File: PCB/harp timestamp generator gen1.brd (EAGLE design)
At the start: 33 x 22 mm, 11 parts, among them IC1 ATXMEGAxxxA4U-AU

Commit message: Updated R1 to 910 ohms.
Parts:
- R1: value 330 -> 910
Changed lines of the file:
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@@
 <attribute name="VALUE" x="32.2834" y="44.831" size="1.27" layer="27"/>
 </element>
-<element name="R1" library="rcl" library_urn="urn:adsk.eagle:library:334" package="R0402" package3d_urn="urn:adsk.eagle:package:23547/3" value="330" x="36.1696" y="46.736" smashed="yes" rot="R180">
+<element name="R1" library="rcl" library_urn="urn:adsk.eagle:library:334" package="R0402" package3d_urn="urn:adsk.eagle:package:23547/3" value="910" x="36.1696" y="46.736" smashed="yes" rot="R180">
 <attribute name="NAME" x="37.084" y="48.1457" size="0.8128" layer="25" font="vector" ratio="12" rot="R180"/>
 <attribute name="POPULARITY" value="0" x="36.1696" y="46.736" size="1.778" layer="27" rot="R180" display="off"/>

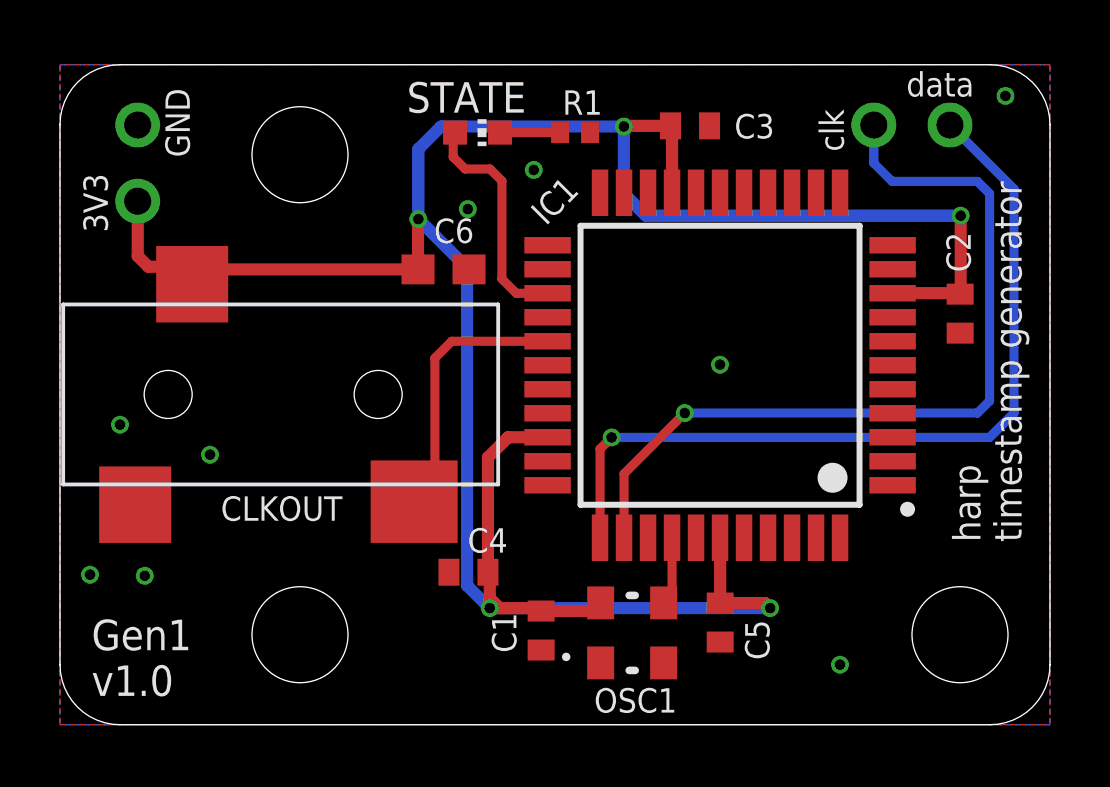
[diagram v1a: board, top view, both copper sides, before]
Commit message: Re-designed oscillator footprint for easier manual assembly
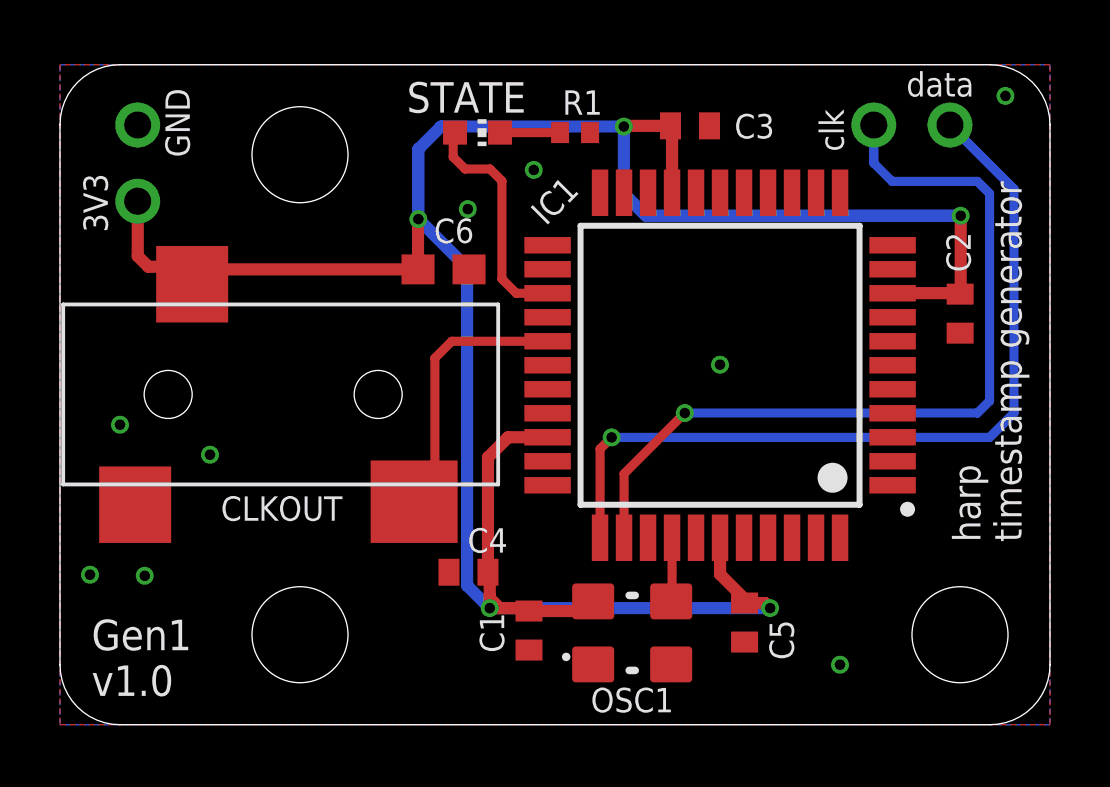
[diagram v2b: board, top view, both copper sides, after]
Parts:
- OSC1: value (none) -> CNP-MISCELLANEOUS_OSCILLATOR; device CNP-miscellaneous:OSCILLATOR_3.2X2.5 -> harp rfid reader v1.0:CNP-MISCELLANEOUS_OSCILLATOR_3.2X2.5
- moved C5 0.81 mm to (41.8, 30.4)
- moved C1 0.41 mm to (34.6, 30.1)
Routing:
- net VCCIO: track 84.5 -> 83.2 mm
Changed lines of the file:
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@@
 <layer number="59" name="tCarbon" color="7" fill="1" visible="no" active="no"/>
 <layer number="60" name="bCarbon" color="7" fill="1" visible="no" active="no"/>
+<layer number="88" name="SimResults" color="9" fill="1" visible="no" active="no"/>
+<layer number="89" name="SimProbes" color="9" fill="1" visible="no" active="no"/>
 <layer number="90" name="Modules" color="7" fill="1" visible="no" active="no"/>
 <layer number="91" name="Nets" color="2" fill="1" visible="no" active="no"/>
@@
 <attribute name="VALUE" x="33.2503" y="33.9863" size="1.27" layer="27" rot="R180"/>
 </element>
-<element name="C5" library="rcl" package="C0402" value="100nF" x="41.0064" y="30.4056" smashed="yes" rot="R270">
-<attribute name="NAME" x="42.651040625" y="29.1574" size="0.8128" layer="25" font="vector" ratio="12" rot="R90"/>
-<attribute name="VALUE" x="39.1014" y="31.0406" size="1.27" layer="27" rot="R270"/>
-</element>
-<element name="OSC1" library="CNP-miscellaneous" package="OSCILLATOR_3.2X2.5" value="" x="38.0732" y="30.06" smashed="yes">
-<attribute name="NAME" x="36.8012625" y="27.403859375" size="0.8128" layer="25" font="vector" ratio="12"/>
-<attribute name="VALUE" x="35.7132" y="27.08" size="1.27" layer="27"/>
-</element>
-<element name="C1" library="rcl" package="C0402" value="100nF" x="35.0388" y="30.1388" smashed="yes" rot="R270">
-<attribute name="NAME" x="33.4005" y="30.7357" size="0.8128" layer="25" font="vector" ratio="12" rot="R270"/>
-<attribute name="VALUE" x="33.1338" y="30.7738" size="1.27" layer="27" rot="R270"/>
+<element name="C5" library="rcl" package="C0402" value="100nF" x="41.8192" y="30.4056" smashed="yes" rot="R270">
+<attribute name="NAME" x="43.463840625" y="29.1574" size="0.8128" layer="25" font="vector" ratio="12" rot="R90"/>
+<attribute name="VALUE" x="39.9142" y="31.0406" size="1.27" layer="27" rot="R270"/>
+</element>
+<element name="C1" library="rcl" package="C0402" value="100nF" x="34.6324" y="30.1388" smashed="yes" rot="R270">
+<attribute name="NAME" x="32.9941" y="30.7357" size="0.8128" layer="25" font="vector" ratio="12" rot="R270"/>
+<attribute name="VALUE" x="32.7274" y="30.7738" size="1.27" layer="27" rot="R270"/>
 </element>
 <element name="CLKOUT" library="CNP-connectors" package="35RASMT2BHNTRX" value="" x="22.605459375" y="38.0087" smashed="yes">
@@
 <attribute name="VALUE" x="36.8046" y="48.641" size="1.27" layer="27" rot="R180"/>
 </element>
+<element name="OSC1" library="harp rfid reader v1.0" package="CNP-MISCELLANEOUS_OSCILLATOR_3.2X2.5" value="CNP-MISCELLANEOUS_OSCILLATOR" x="38.0732" y="30.06" smashed="yes">
+<attribute name="NAME" x="36.6895" y="27.414021875" size="0.8128" layer="25" font="vector" ratio="15"/>
+<attribute name="VALUE" x="35.7132" y="27.08" size="1.27" layer="27"/>
+</element>
 </elements>
 <signals>
 <signal name="GND">
-<contactref element="OSC1" pad="P$2"/>
 <contactref element="C1" pad="2"/>
 <contactref element="IC1" pad="8"/>
@@
 <contactref element="R1" pad="1"/>
 <via x="34.793240625" y="45.492759375" extent="1-16" drill="0.35"/>
+<contactref element="OSC1" pad="P$2"/>
+<wire x1="49.004440625" y1="40.05218125" x2="50.515621875" y2="47.959359375" width="0" layer="19" extent="1-1"/>
+<wire x1="46.752" y1="40.5816" x2="49.004440625" y2="40.05218125" width="0" layer="19" extent="1-1"/>
+<wire x1="41" y1="39" x2="46.752" y2="40.5816" width="0" layer="19" extent="1-1"/>
+<wire x1="40.202" y1="44.7316" x2="41" y2="39" width="0" layer="19" extent="1-1"/>
+<wire x1="40.650759375" y1="46.961421875" x2="40.202" y2="44.7316" width="0" layer="19" extent="1-1"/>
+<wire x1="36.6696" y1="46.736" x2="40.650759375" y2="46.961421875" width="0" layer="19" extent="1-1"/>
+<wire x1="34.793240625" y1="45.492759375" x2="36.6696" y2="46.736" width="0" layer="19" extent="1-1"/>
+<wire x1="32.5936" y1="44.1872" x2="34.793240625" y2="45.492759375" width="0" layer="19" extent="1-1"/>
+<wire x1="32.6349" y1="42.1775" x2="32.5936" y2="44.1872" width="0" layer="19" extent="1-1"/>
+<wire x1="35.252" y1="37.3816" x2="32.6349" y2="42.1775" width="0" layer="19" extent="1-1"/>
+<wire x1="40.202" y1="33.2316" x2="41" y2="39" width="0" layer="19" extent="1-1"/>
+<wire x1="41.8192" y1="29.7556" x2="40.202" y2="33.2316" width="0" layer="19" extent="1-1"/>
+<wire x1="39.3732" y1="29.01" x2="41.8192" y2="29.7556" width="0" layer="19" extent="1-1"/>
+<wire x1="45" y1="29" x2="41.8192" y2="29.7556" width="0" layer="19" extent="1-1"/>
+<wire x1="34.6324" y1="29.4888" x2="39.3732" y2="29.01" width="0" layer="19" extent="1-1"/>
+<wire x1="31.9653" y1="32.0813" x2="34.6324" y2="29.4888" width="0" layer="19" extent="1-1"/>
+<wire x1="24" y1="36" x2="31.9653" y2="32.0813" width="0" layer="19" extent="1-1"/>
+<wire x1="21.505459375" y1="34.3337" x2="24" y2="36" width="0" layer="19" extent="1-1"/>
+<wire x1="21.8255" y1="31.96418125" x2="21.505459375" y2="34.3337" width="0" layer="19" extent="1-1"/>
+<wire x1="20" y1="32" x2="21.8255" y2="31.96418125" width="0" layer="19" extent="1-1"/>
+<wire x1="21" y1="37" x2="21.505459375" y2="34.3337" width="0" layer="19" extent="1-1"/>
+<wire x1="21.59" y1="46.99" x2="21" y2="37" width="0" layer="19" extent="1-1"/>
 </signal>
 <signal name="VCCIO">
@@
 <contactref element="C2" pad="1"/>
 <contactref element="C3" pad="1"/>
-<contactref element="OSC1" pad="P$4"/>
 <contactref element="C1" pad="1"/>
 <contactref element="C5" pad="1"/>
@@
 <wire x1="33.3248" y1="30.8864" x2="32.57041875" y2="31.64078125" width="0.4064" layer="16"/>
 <wire x1="32.57041875" y1="42.2275" x2="30.94481875" y2="43.8531" width="0.4064" layer="16"/>
-<wire x1="35.0388" y1="30.7888" x2="34.9412" y2="30.8864" width="0.4064" layer="1"/>
-<wire x1="34.9412" y1="30.8864" x2="33.7312" y2="30.8864" width="0.4064" layer="1"/>
+<wire x1="34.6324" y1="30.7888" x2="34.5348" y2="30.8864" width="0.4064" layer="1"/>
+<wire x1="34.5348" y1="30.8864" x2="33.7312" y2="30.8864" width="0.4064" layer="1"/>
 <wire x1="33.7312" y1="30.8864" x2="33.3248" y2="30.8864" width="0.4064" layer="1"/>
-<wire x1="41.0064" y1="31.0556" x2="42.5028" y2="31.0556" width="0.4064" layer="1"/>
+<wire x1="41.8192" y1="31.0556" x2="42.5028" y2="31.0556" width="0.4064" layer="1"/>
 <wire x1="42.5028" y1="31.0556" x2="42.672" y2="30.8864" width="0.4064" layer="1"/>
 <via x="42.672" y="30.8864" extent="1-16" drill="0.35"/>
@@
 <wire x1="46.755821875" y1="41.385421875" x2="48.9712" y2="41.385421875" width="0.4064" layer="1"/>
 <wire x1="48.9712" y1="41.385421875" x2="49.022859375" y2="41.385421875" width="0.4064" layer="1"/>
-<wire x1="41.002" y1="33.2316" x2="41.0064" y2="33.2272" width="0.4064" layer="1"/>
-<wire x1="41.0064" y1="33.2272" x2="41.0064" y2="31.0556" width="0.4064" layer="1"/>
-<wire x1="37.0232" y1="31.06" x2="36.752" y2="30.7888" width="0.4064" layer="1"/>
-<wire x1="36.752" y1="30.7888" x2="35.0388" y2="30.7888" width="0.4064" layer="1"/>
+<wire x1="41.8192" y1="31.1952" x2="41.002" y2="32.0124" width="0.4064" layer="1"/>
+<wire x1="41.002" y1="33.2316" x2="41.002" y2="32.0124" width="0.4064" layer="1"/>
+<wire x1="41.8192" y1="31.1952" x2="41.8192" y2="31.0556" width="0.4064" layer="1"/>
+<wire x1="36.3456" y1="30.7888" x2="34.6324" y2="30.7888" width="0.4064" layer="1"/>
 <wire x1="33.2653" y1="32.0813" x2="33.2653" y2="35.9069" width="0.4064" layer="1"/>
 <wire x1="33.94" y1="36.5816" x2="35.252" y2="36.5816" width="0.4064" layer="1"/>
@@
 <wire x1="23.164803125" y1="42.2656" x2="23.57608125" y2="41.854321875" width="0.3048" layer="1"/>
 <wire x1="21.9456" y1="42.2656" x2="23.164803125" y2="42.2656" width="0.4064" layer="1"/>
+<contactref element="OSC1" pad="P$4"/>
+<wire x1="36.3456" y1="30.7888" x2="36.7732" y2="31.11" width="0" layer="19" extent="1-1"/>
 </signal>
 <signal name="N$17">
@@
 </signal>
 <signal name="OSC1">
-<contactref element="OSC1" pad="P$3"/>
 <contactref element="IC1" pad="37"/>
 <wire x1="39.402" y1="33.2316" x2="39.402" y2="31.3388" width="0.3048" layer="1"/>
-<wire x1="39.402" y1="31.3388" x2="39.1232" y2="31.06" width="0.3048" layer="1"/>
+<contactref element="OSC1" pad="P$3"/>
+<wire x1="39.3732" y1="31.11" x2="39.402" y2="31.3388" width="0" layer="19" extent="1-1"/>
 </signal>
 <signal name="GND2">
